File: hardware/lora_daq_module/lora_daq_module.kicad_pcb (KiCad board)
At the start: 4 copper layers, 70 x 40 mm, 64 parts, among them J1 JST3pinfemale, J2 SMA_Edge_50Ω, J3 USB_C_Receptacle_USB2.0_14P, J4 EXT_UART, J5 SWD, J6 Micro_SD_Card_Det1, J7 Conn_01x02, U1 OPA333, U2 ADS1115IDGS, U3 CP2102N-Axx-xQFN20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

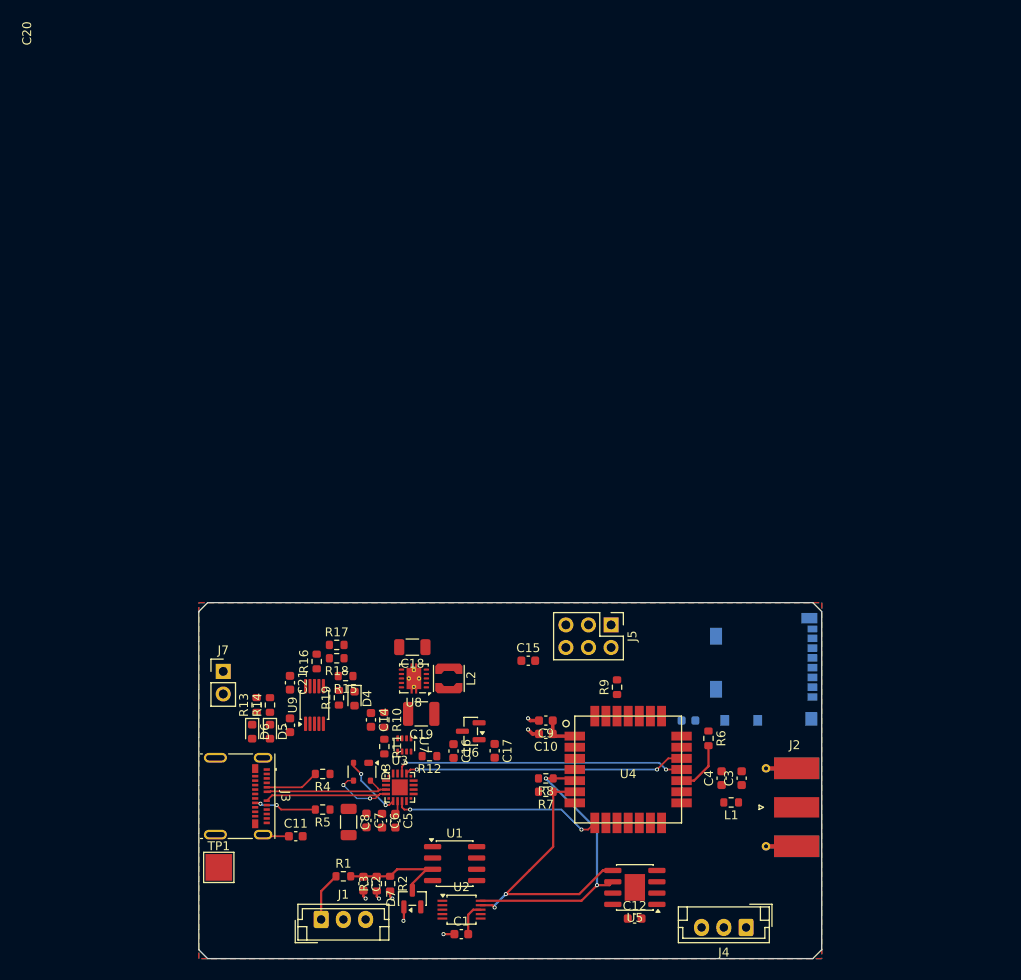
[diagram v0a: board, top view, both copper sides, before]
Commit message: near-complete layout of power domain
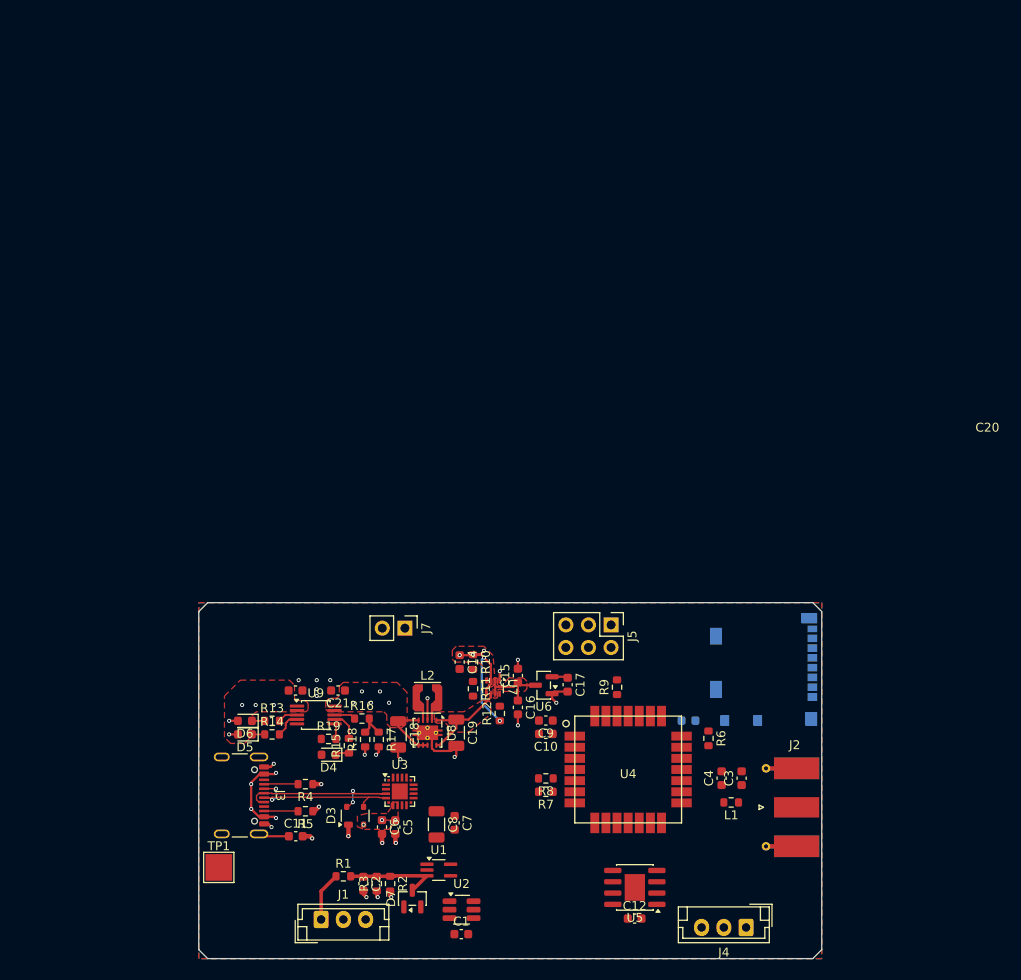
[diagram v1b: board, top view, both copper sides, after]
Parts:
- C1: value 0.1uF -> .1u
- C14: value .47u -> 47n
- C18: value 10uF -> 10u
- C19: value 33uF -> 33u; footprint Capacitor_SMD:C_1210_3225Metric -> Capacitor_SMD:C_1206_3216Metric
- C2: value 47nF -> 47n
- C20, C21: value 1uF -> 1u
- D4: value ~ -> Green
- D5: value ~ -> Yellow
- D6: value ~ -> Red
- J3: footprint Connector_USB:USB_C_Receptacle_Molex_105450-0101 -> Connector_USB:USB_C_Receptacle_GCT_USB4105-xx-A_16P_TopMnt_Horizontal
- L1: value 0 -> 50Ω
- R13, R14, R15: value 470Ω -> 470
- R16, R19: value 1kΩ -> 1k
- U1: footprint Package_SO:SOIC-8_3.9x4.9mm_P1.27mm -> Package_TO_SOT_SMD:SOT-353_SC-70-5_Handsoldering
- U2: value ADS1115IDGS -> ADS1110A0IDBVR; footprint Package_SO:TSSOP-10_3x3mm_P0.5mm -> Package_TO_SOT_SMD:SOT-23-6_Handsoldering
- moved J7 21.0 mm to (130.8, 85.6), turned to -90 degrees
- moved C14 11.9 mm to (137.0, 89.4)
- moved R10 11.9 mm to (138.5, 89.4)
- moved R11 11.9 mm to (138.5, 92.4)
- moved U7 11.9 mm to (140.7, 92.2)
- moved R17 11.6 mm to (127.9, 98.1), turned to -90 degrees
- moved C17 11.1 mm to (149.1, 91.9)
- moved C18 9.94 mm to (130.0, 97.5), turned to -90 degrees
- moved C7 9.91 mm to (136.4, 107.5)
- moved C8 9.88 mm to (134.4, 107.6)
- moved U6 9.69 mm to (146.4, 92.0)
- moved R18 9.67 mm to (126.3, 98.1), turned to 90 degrees
- moved R12 9.24 mm to (141.5, 95.2), turned to 90 degrees
- moved C16 8.74 mm to (143.5, 94.5)
- moved R16 8.19 mm to (126.0, 95.8), turned to 0 degrees
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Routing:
- net SCL: track 33.5 -> 0.00 mm, vias 2 -> 0
- net SDA: track 33.0 -> 0.00 mm, vias 2 -> 0
- net RX1: track 32.7 -> 0.00 mm, vias 2 -> 0
- net TX1: track 31.6 -> 0.00 mm, vias 2 -> 0
- net USB_RST: track 23.7 -> 0.00 mm, vias 2 -> 0
- net GND: track 8.48 -> 29.6 mm, vias 7 -> 25
- net VBUS: track 8.80 -> 29.9 mm, vias 2 -> 17
- net +5V_bat: track 0.00 -> 11.6 mm
- net +5V: track 0.00 -> 8.34 mm
- net D+: track 15.1 -> 22.2 mm, vias 0 -> 2
- net +VBATT: track 0.00 -> 7.10 mm, vias 0 -> 5
- net +3.3V: track 7.90 -> 1.80 mm
- net Net-(U4-F5/~{RST}): track 6.00 -> 0.00 mm
- net Net-(R16-Pad2): track 0.00 -> 3.68 mm
- net Net-(U9-~{PG}): track 0.00 -> 3.30 mm
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- added copper zone on F.Cu, net +5V
- added copper zone on F.Cu, net +5V_bat
- added copper zone on F.Cu, net +VBATT
- added copper zone on F.Cu, net VBUS
- added copper zone on In2.Cu, net VBUS

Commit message: lay traces to all components
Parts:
- added R20: 0, Resistor_SMD:R_0603_1608Metric, F.Cu at (138.8, 104.2)
- TP1: footprint TestPoint:TestPoint_Pad_3.0x3.0mm -> TestPoint:TestPoint_Pad_1.5x1.5mm
- U2: footprint Package_TO_SOT_SMD:SOT-23-6_Handsoldering -> Package_TO_SOT_SMD:SOT-23-6
- moved TP1 27.3 mm to (135.8, 104.0)
- moved C13 6.10 mm to (168.2, 98.6), turned to -90 degrees
- moved C1 4.39 mm to (140.2, 116.8), turned to 180 degrees
- moved C3 2.25 mm to (166.4, 102.4)
- moved C4 2.20 mm to (168.6, 102.4)
- moved C7 0.50 mm to (136.4, 107.0)
- moved U2 0.46 mm to (137.0, 116.8), turned to 90 degrees
- turned L1 to 0 degrees
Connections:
- net Net-(U3-VDD) renamed vreg
- D7 pad 2: +5V -> +3.3V
- U2 pad 1: GND -> Net-(U1--)
- U2 pad 2: ADC_ALRT -> GND
- U2 pad 3: GND -> SCL
- U2 pad 4: Net-(U1--) -> SDA
- U2 pad 5: unconnected-(U2-AIN1-Pad5) -> +3.3V
- U2 pad 6: unconnected-(U2-AIN2-Pad6) -> GND
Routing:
- net SDDO: track 0.00 -> 35.5 mm, vias 0 -> 1
- net RX1: track 0.00 -> 32.9 mm, vias 0 -> 2
- net TX1: track 0.00 -> 32.2 mm, vias 0 -> 2
- net SCL: track 0.00 -> 32.0 mm, vias 0 -> 3
- net SDDI: track 0.00 -> 31.1 mm, vias 0 -> 1
- net SDA: track 0.00 -> 29.7 mm
- net SDCLK: track 0.00 -> 26.9 mm, vias 0 -> 1
- net SDCS: track 0.00 -> 26.0 mm, vias 0 -> 1
- net USB_RST: track 0.00 -> 25.2 mm, vias 0 -> 4
- net GND: track 29.6 -> 54.2 mm, vias 25 -> 40
- net +3.3V: track 1.80 -> 24.7 mm, vias 0 -> 13
- net EXT_TX: track 0.00 -> 20.6 mm, vias 0 -> 1
- net EXT_RX: track 0.00 -> 19.5 mm, vias 0 -> 1
- net SWDCLK: track 0.00 -> 16.1 mm, vias 0 -> 1
- net SWDIO: track 0.00 -> 14.9 mm, vias 0 -> 1
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- added copper zone on F.Cu, net +3.3V
- added copper zone on In2.Cu, net +3.3V
- added copper zone on F.Cu, net vreg

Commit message: finish rough layout, drc fixedup
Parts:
- moved C13 4.73 mm to (163.8, 96.8), turned to 90 degrees
- moved J2 0.19 mm to (172.9, 105.7)
- moved D5 0.11 mm to (112.9, 97.6)
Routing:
- net GND: track 54.2 -> 66.2 mm, vias 40 -> 45
- net Net-(U7-PR1): track 0.00 -> 2.89 mm
- net VBUS_READY: track 0.00 -> 1.40 mm
- net Net-(J6-SHIELD): track 2.43 -> 3.57 mm
- added copper zone on In2.Cu, net +VBATT
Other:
- board text added: "+"
- board text added: "+3.3v"
- board text added: "-"
- board text added: "adc1"
- board text added: "batt"
- board text added: "chrg"
- board text added: "clk"
- board text added: "dio"
- board text added: "gnd"
- board text added: "lora_daq_module"
- board text added: "psu_capstone_team14"
- board text added: "rev1 fall25"
- board text added: "thrm"
- board text added: "uart1"

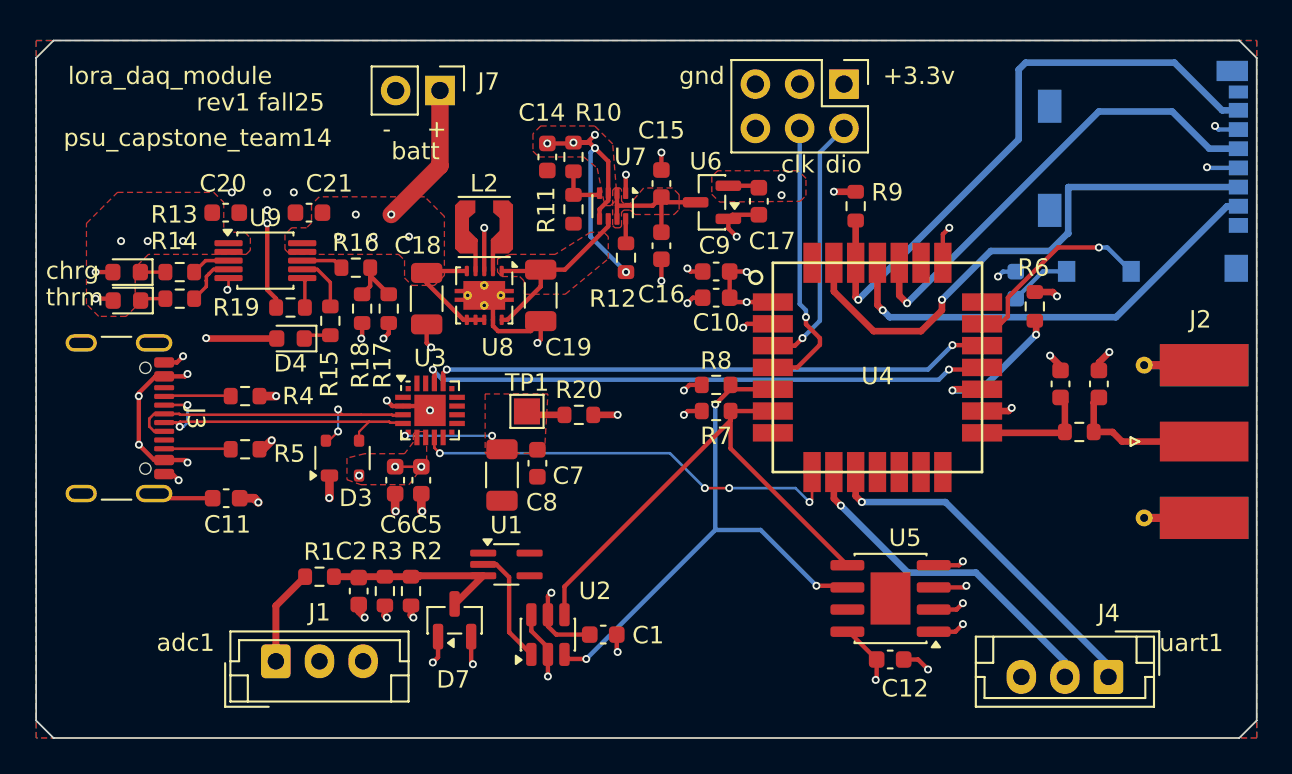
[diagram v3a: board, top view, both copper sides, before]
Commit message: add test points and antenna microstrip
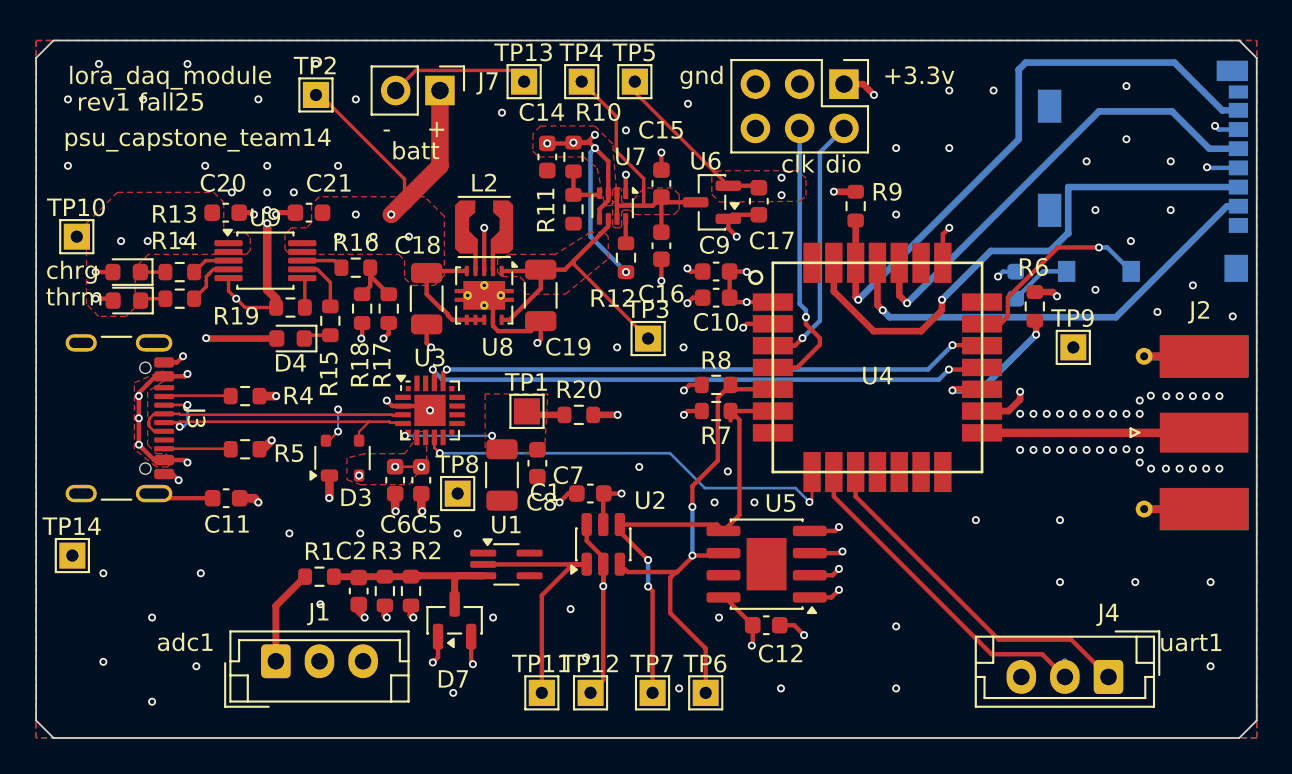
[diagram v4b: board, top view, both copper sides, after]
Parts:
- removed C3, C4: 0, Capacitor_SMD:C_0603_1608Metric
- removed L1: 50Ω, Resistor_SMD:R_0603_1608Metric
- added TP10: tp_vbus, TestPoint:TestPoint_THTPad_1.5x1.5mm_Drill0.7mm, F.Cu at (110.0, 94.0)
- added TP11: tp_sig+, TestPoint:TestPoint_THTPad_1.5x1.5mm_Drill0.7mm, F.Cu at (136.7, 120.1)
- added TP12: tp_siggnd, TestPoint:TestPoint_THTPad_1.5x1.5mm_Drill0.7mm, F.Cu at (139.4, 120.1)
- added TP13: tp_batgnd, TestPoint:TestPoint_THTPad_1.5x1.5mm_Drill0.7mm, F.Cu at (135.6, 85.1)
- added TP14: tp_usbgnd, TestPoint:TestPoint_THTPad_1.5x1.5mm_Drill0.7mm, F.Cu at (109.7, 112.3)
- added TP2: tp_vbatt, TestPoint:TestPoint_THTPad_1.5x1.5mm_Drill0.7mm, F.Cu at (123.7, 85.9)
- added TP3: tp_5vbatt, TestPoint:TestPoint_THTPad_1.5x1.5mm_Drill0.7mm, F.Cu at (142.7, 99.8)
- added TP4: tp_5v, TestPoint:TestPoint_THTPad_1.5x1.5mm_Drill0.7mm, F.Cu at (138.9, 85.1)
- added TP5: tp_3v3, TestPoint:TestPoint_THTPad_1.5x1.5mm_Drill0.7mm, F.Cu at (142.0, 85.1)
- added TP6: tp_scl, TestPoint:TestPoint_THTPad_1.5x1.5mm_Drill0.7mm, F.Cu at (146.1, 120.1)
- added TP7: tp_sda, TestPoint:TestPoint_THTPad_1.5x1.5mm_Drill0.7mm, F.Cu at (143.0, 120.1)
- added TP8: tp_rusb, TestPoint:TestPoint_THTPad_1.5x1.5mm_Drill0.7mm, F.Cu at (131.8, 108.7)
- added TP9: tp_rstup, TestPoint:TestPoint_THTPad_1.5x1.5mm_Drill0.7mm, F.Cu at (167.1, 100.3)
- moved C1 8.12 mm to (139.4, 108.7), turned to 0 degrees
- moved C12 7.37 mm to (149.5, 116.3)
- moved U5 7.37 mm to (149.5, 112.8)
- moved U2 6.07 mm to (140.2, 111.6)
- moved J2 0.51 mm to (172.9, 105.2)
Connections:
- U4 pad 15: Net-(U4-RFIO) -> Net-(J2-In)
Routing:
- net GND: track 66.2 -> 86.0 mm, vias 45 -> 140
- net +VBATT: track 15.4 -> 24.1 mm
- net +5V: track 8.34 -> 16.9 mm
- net +3.3V: track 24.7 -> 33.1 mm, vias 13 -> 14
- net Net-(U1--): track 6.74 -> 14.8 mm
- net Net-(U4-RFIO): track 6.85 -> 0.00 mm
- net +5V_bat: track 11.6 -> 17.9 mm
- net Net-(J2-In): track 8.86 -> 13.6 mm
- net SCL: track 32.0 -> 28.2 mm, vias 3 -> 2
- net SDA: track 29.7 -> 27.0 mm, vias 0 -> 2
- net Net-(U1-+): track 10.9 -> 11.8 mm
- net EXT_TX: track 20.6 -> 20.9 mm, vias 1 -> 0
- net EXT_RX: track 19.5 -> 19.8 mm, vias 1 -> 0
- net VBUS: vias 18 -> 19
- net USB_RST: vias 4 -> 2
